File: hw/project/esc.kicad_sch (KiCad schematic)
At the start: 0 parts

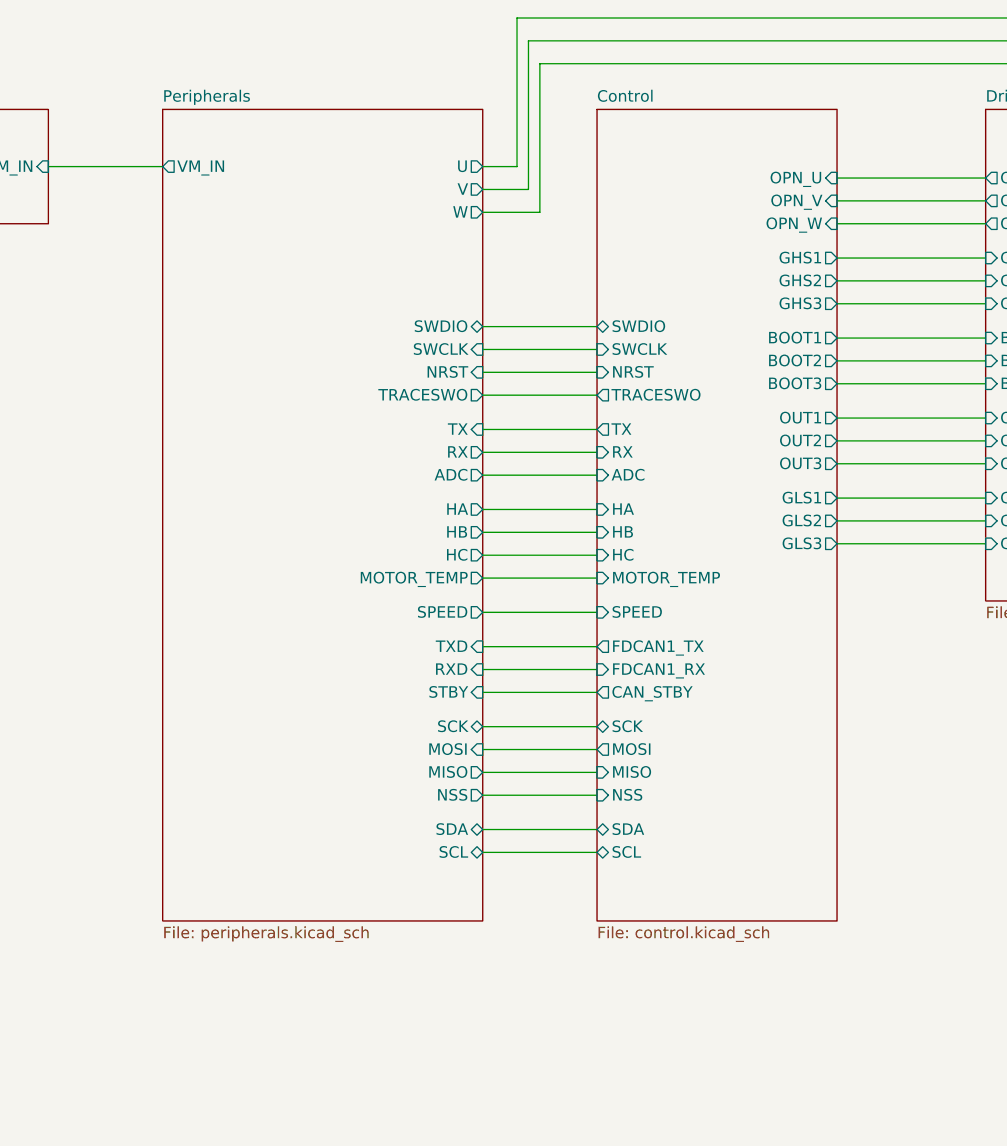
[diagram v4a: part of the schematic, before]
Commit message: Wire up status leds
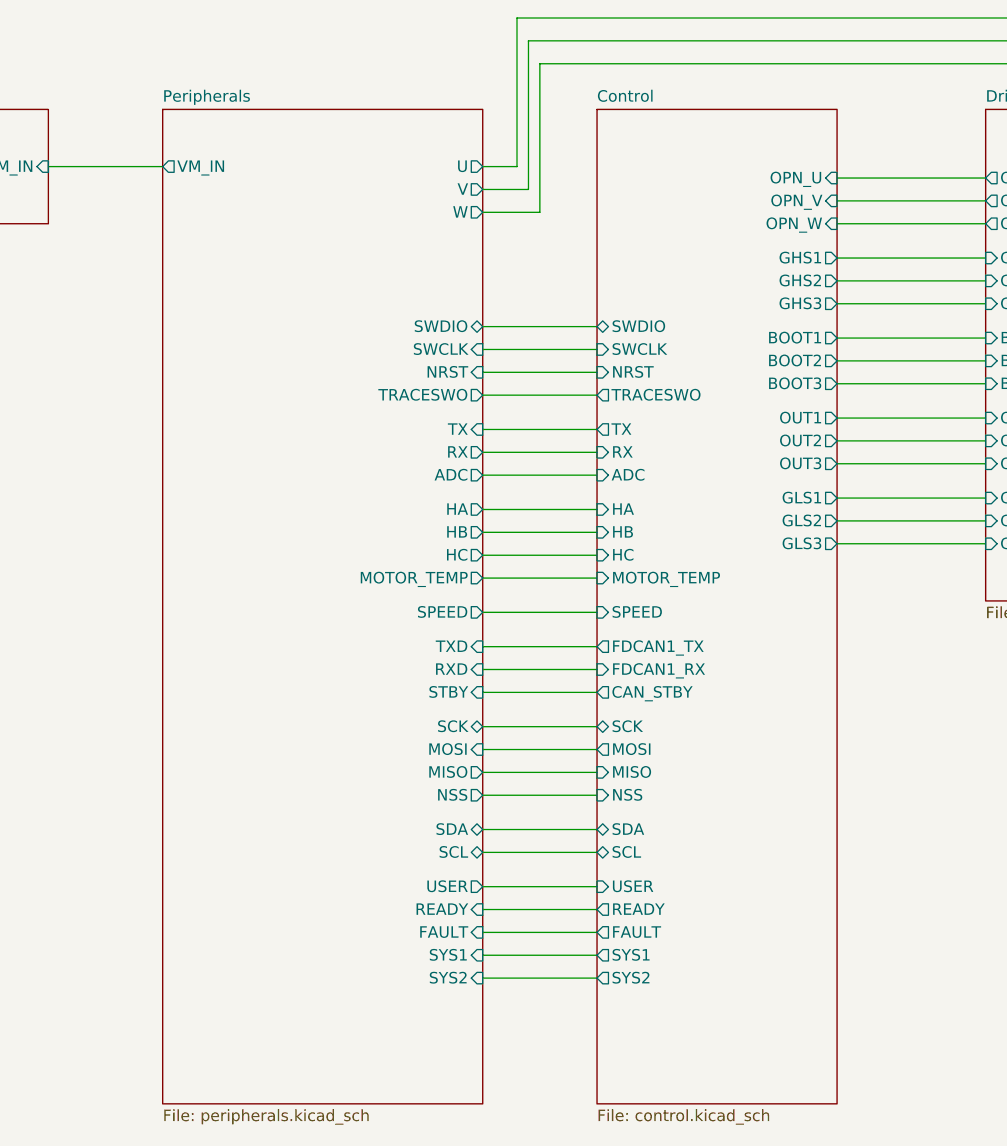
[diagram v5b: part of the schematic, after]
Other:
- sheet Control ports: added FAULT, READY, SYS1, SYS2, USER; removed none
- sheet Peripherals ports: added FAULT, READY, SYS1, SYS2, USER; removed none
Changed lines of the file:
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@@
+	(wire
+		(pts
+			(xy 152.4 156.21) (xy 165.1 156.21)
+		)
+		(stroke
+			(width 0)
+			(type default)
+		)
+	)
 	(wire
 		(pts
@@
 	(wire
 		(pts
+			(xy 152.4 158.75) (xy 165.1 158.75)
+		)
+		(stroke
+			(width 0)
+			(type default)
+		)
+	)
+	(wire
+		(pts
 			(xy 208.28 97.79) (xy 191.77 97.79)
 		)
@@
 	(wire
 		(pts
+			(xy 152.4 161.29) (xy 165.1 161.29)
+		)
+		(stroke
+			(width 0)
+			(type default)
+		)
+	)
+	(wire
+		(pts
 			(xy 157.48 76.2) (xy 152.4 76.2)
 		)
@@
 	(wire
 		(pts
+			(xy 152.4 153.67) (xy 165.1 153.67)
+		)
+		(stroke
+			(width 0)
+			(type default)
+		)
+	)
+	(wire
+		(pts
 			(xy 165.1 93.98) (xy 152.4 93.98)
+		)
+		(stroke
+			(width 0)
+			(type default)
+		)
+	)
+	(wire
+		(pts
+			(xy 152.4 163.83) (xy 165.1 163.83)
 		)
 		(stroke
@@
 	(sheet
 		(at 165.1 67.31)
-		(size 26.67 90.17)
+		(size 26.67 110.49)
 		(exclude_from_sim no)
 		(in_bom yes)
@@
 		)
 		(property "Sheetfile" "control.kicad_sch"
-			(at 165.1 158.0646 0)
+			(at 165.1 178.3846 0)
 			(show_name no)
 			(do_not_autoplace no)
@@
 		(pin "SDA" bidirectional
 			(at 165.1 147.32 180)
+			(effects
+				(font
+					(size 1.27 1.27)
+				)
+				(justify left)
+			)
+		)
+		(pin "SYS2" output
+			(at 165.1 163.83 180)
+			(effects
+				(font
+					(size 1.27 1.27)
+				)
+				(justify left)
+			)
+		)
+		(pin "SYS1" output
+			(at 165.1 161.29 180)
+			(effects
+				(font
+					(size 1.27 1.27)
+				)
+				(justify left)
+			)
+		)
+		(pin "FAULT" output
+			(at 165.1 158.75 180)
+			(effects
+				(font
+					(size 1.27 1.27)
+				)
+				(justify left)
+			)
+		)
+		(pin "USER" input
+			(at 165.1 153.67 180)
+			(effects
+				(font
+					(size 1.27 1.27)
+				)
+				(justify left)
+			)
+		)
+		(pin "READY" output
+			(at 165.1 156.21 180)
 			(effects
 				(font
@@
 	(sheet
 		(at 116.84 67.31)
-		(size 35.56 90.17)
+		(size 35.56 110.49)
 		(exclude_from_sim no)
 		(in_bom yes)
@@
 		)
 		(property "Sheetfile" "peripherals.kicad_sch"
-			(at 116.84 158.0646 0)
+			(at 116.84 178.3846 0)
 			(show_name no)
 			(do_not_autoplace no)
@@
 			(effects
 				(font
+					(size 1.27 1.27)
+				)
+				(justify right)
+			)
+		)
+		(pin "USER" output
+			(at 152.4 153.67 0)
+			(effects
+				(font
+					(size 1.27 1.27)
+				)
+				(justify right)
+			)
+		)
+		(pin "SYS1" input
+			(at 152.4 161.29 0)
+			(effects
+				(font
+					(size 1.27 1.27)
+				)
+				(justify right)
+			)
+		)
+		(pin "SYS2" input
+			(at 152.4 163.83 0)
+			(effects
+				(font
+					(size 1.27 1.27)
+				)
+				(justify right)
+			)
+		)
+		(pin "READY" input
+			(at 152.4 156.21 0)
+			(effects
+				(font
+					(size 1.27 1.27)
+				)
+				(justify right)
+			)
+		)
+		(pin "FAULT" input
+			(at 152.4 158.75 0)
+			(effects
+				(font

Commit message: stm header and minor changes
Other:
- sheet Control ports: added PA1, PA2, PA8, PB1, PB6, PB7, PC2; removed none

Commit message: minor changes
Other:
- sheet Control ports: added PWR_BTN; removed PB1, PB6
- sheet Peripherals ports: added PA1, PA2, PA8, PB7, PC2, PWR_BTN; removed none
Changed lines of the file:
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@@
+	(wire
+		(pts
+			(xy 118.11 154.94) (xy 130.81 154.94)
+		)
+		(stroke
+			(width 0)
+			(type default)
+		)
+	)
 	(wire
 		(pts
@@
 	(wire
 		(pts
+			(xy 118.11 158.75) (xy 130.81 158.75)
+		)
+		(stroke
+			(width 0)
+			(type default)
+		)
+	)
+	(wire
+		(pts
 			(xy 173.99 54.61) (xy 157.48 54.61)
 		)
@@
 	(wire
 		(pts
+			(xy 118.11 139.7) (xy 130.81 139.7)
+		)
+		(stroke
+			(width 0)
+			(type default)
+		)
+	)
+	(wire
+		(pts
 			(xy 189.23 27.94) (xy 121.92 27.94)
 		)
@@
 	(wire
 		(pts
+			(xy 118.11 147.32) (xy 130.81 147.32)
+		)
+		(stroke
+			(width 0)
+			(type default)
+		)
+	)
+	(wire
+		(pts
 			(xy 123.19 46.99) (xy 118.11 46.99)
 		)
@@
 	(wire
 		(pts
+			(xy 118.11 144.78) (xy 130.81 144.78)
+		)
+		(stroke
+			(width 0)
+			(type default)
+		)
+	)
+	(wire
+		(pts
 			(xy 130.81 64.77) (xy 118.11 64.77)
 		)
@@
 		(pts
 			(xy 118.11 134.62) (xy 130.81 134.62)
+		)
+		(stroke
+			(width 0)
+			(type default)
+		)
+	)
+	(wire
+		(pts
+			(xy 118.11 152.4) (xy 130.81 152.4)
 		)
 		(stroke
@@
 			)
 		)
-		(pin "PB1" input
-			(at 130.81 142.24 180)
-			(effects
-				(font
-					(size 1.27 1.27)
-				)
-				(justify left)
-			)
-		)
 		(pin "PA1" input
 			(at 130.81 144.78 180)
@@
 			)
 		)
-		(pin "PB6" input
-			(at 130.81 149.86 180)
-			(effects
-				(font
-					(size 1.27 1.27)
-				)
-				(justify left)
-			)
-		)
 		(pin "PA8" input
 			(at 130.81 152.4 180)
@@
 		(pin "PC2" input
 			(at 130.81 154.94 180)
+			(effects
+				(font
+					(size 1.27 1.27)
+				)
+				(justify left)
+			)
+		)
+		(pin "PWR_BTN" input
+			(at 130.81 158.75 180)
 			(effects
 				(font
@@
 			(effects
 				(font
+					(size 1.27 1.27)
+				)
+				(justify right)
+			)
+		)
+		(pin "PA1" input
+			(at 118.11 144.78 0)
+			(effects
+				(font
+					(size 1.27 1.27)
+				)
+				(justify right)
+			)
+		)
+		(pin "PC2" input
+			(at 118.11 154.94 0)
+			(effects
+				(font
+					(size 1.27 1.27)
+				)
+				(justify right)
+			)
+		)
+		(pin "PA2" input
+			(at 118.11 139.7 0)
+			(effects
+				(font
+					(size 1.27 1.27)
+				)
+				(justify right)
+			)
+		)
+		(pin "PA8" input
+			(at 118.11 152.4 0)
+			(effects
+				(font
+					(size 1.27 1.27)
+				)
+				(justify right)
+			)
+		)
+		(pin "PB7" input
+			(at 118.11 147.32 0)
+			(effects
+				(font
+					(size 1.27 1.27)
+				)
+				(justify right)
+			)
+		)
+		(pin "PWR_BTN" output
+			(at 118.11 158.75 0)
+			(effects
+				(font

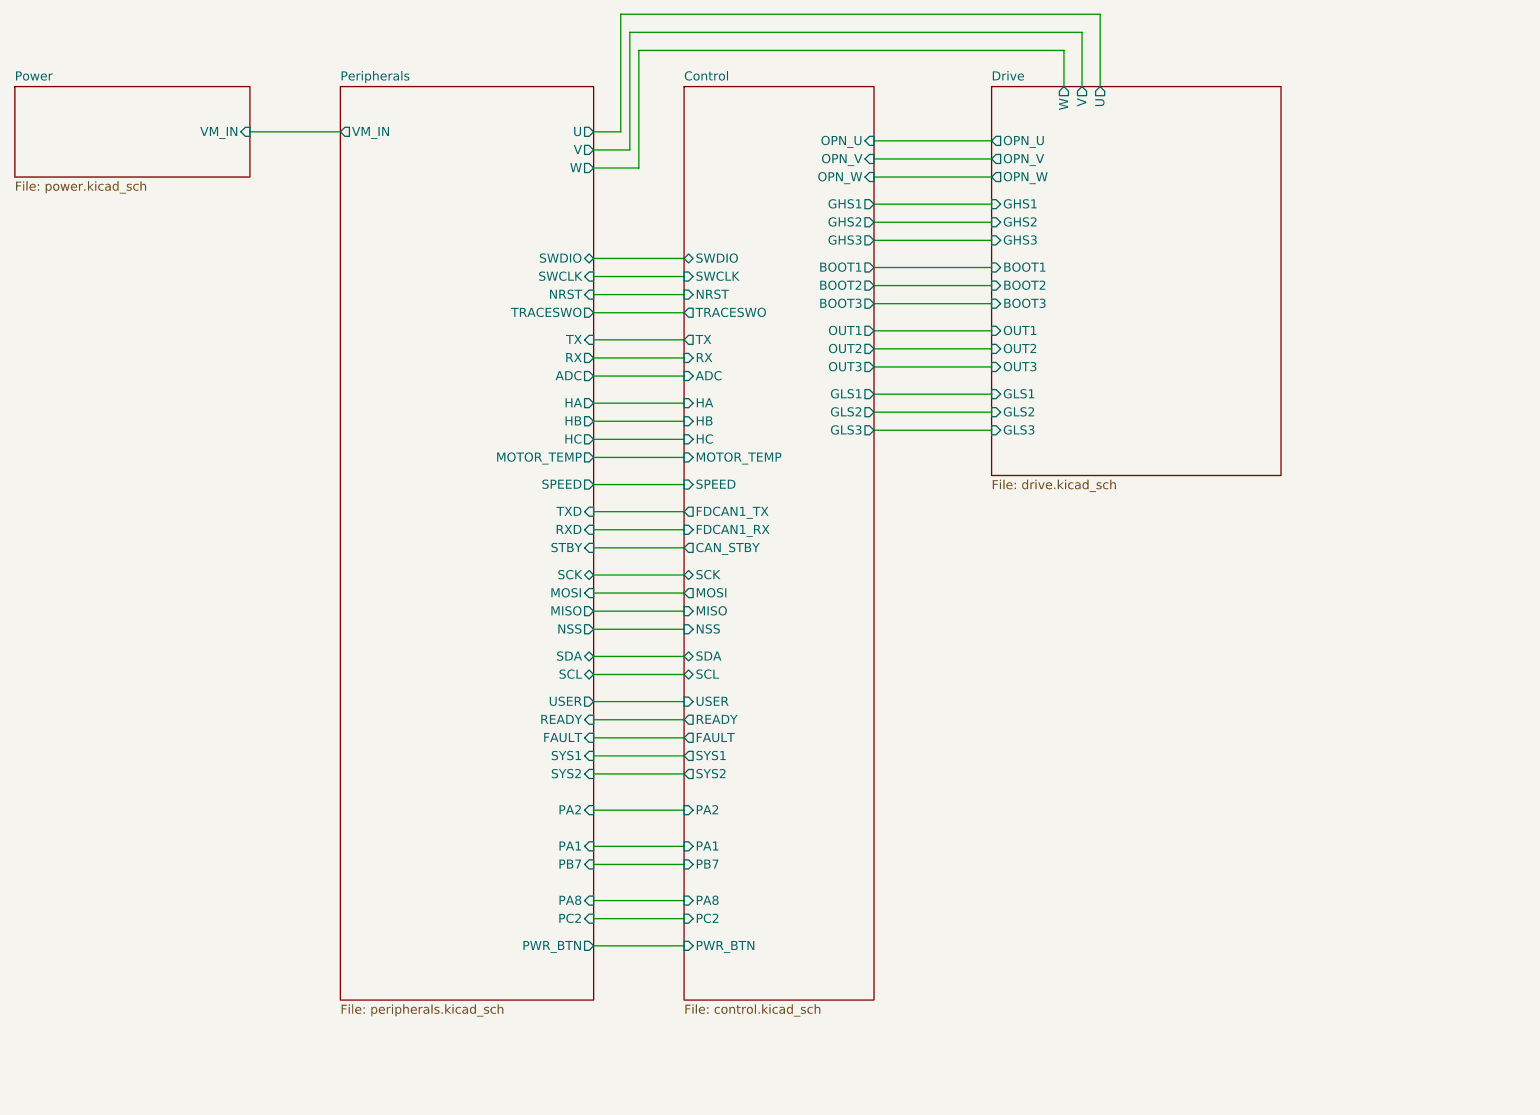
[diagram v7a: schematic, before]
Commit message: Wire PWR BTN
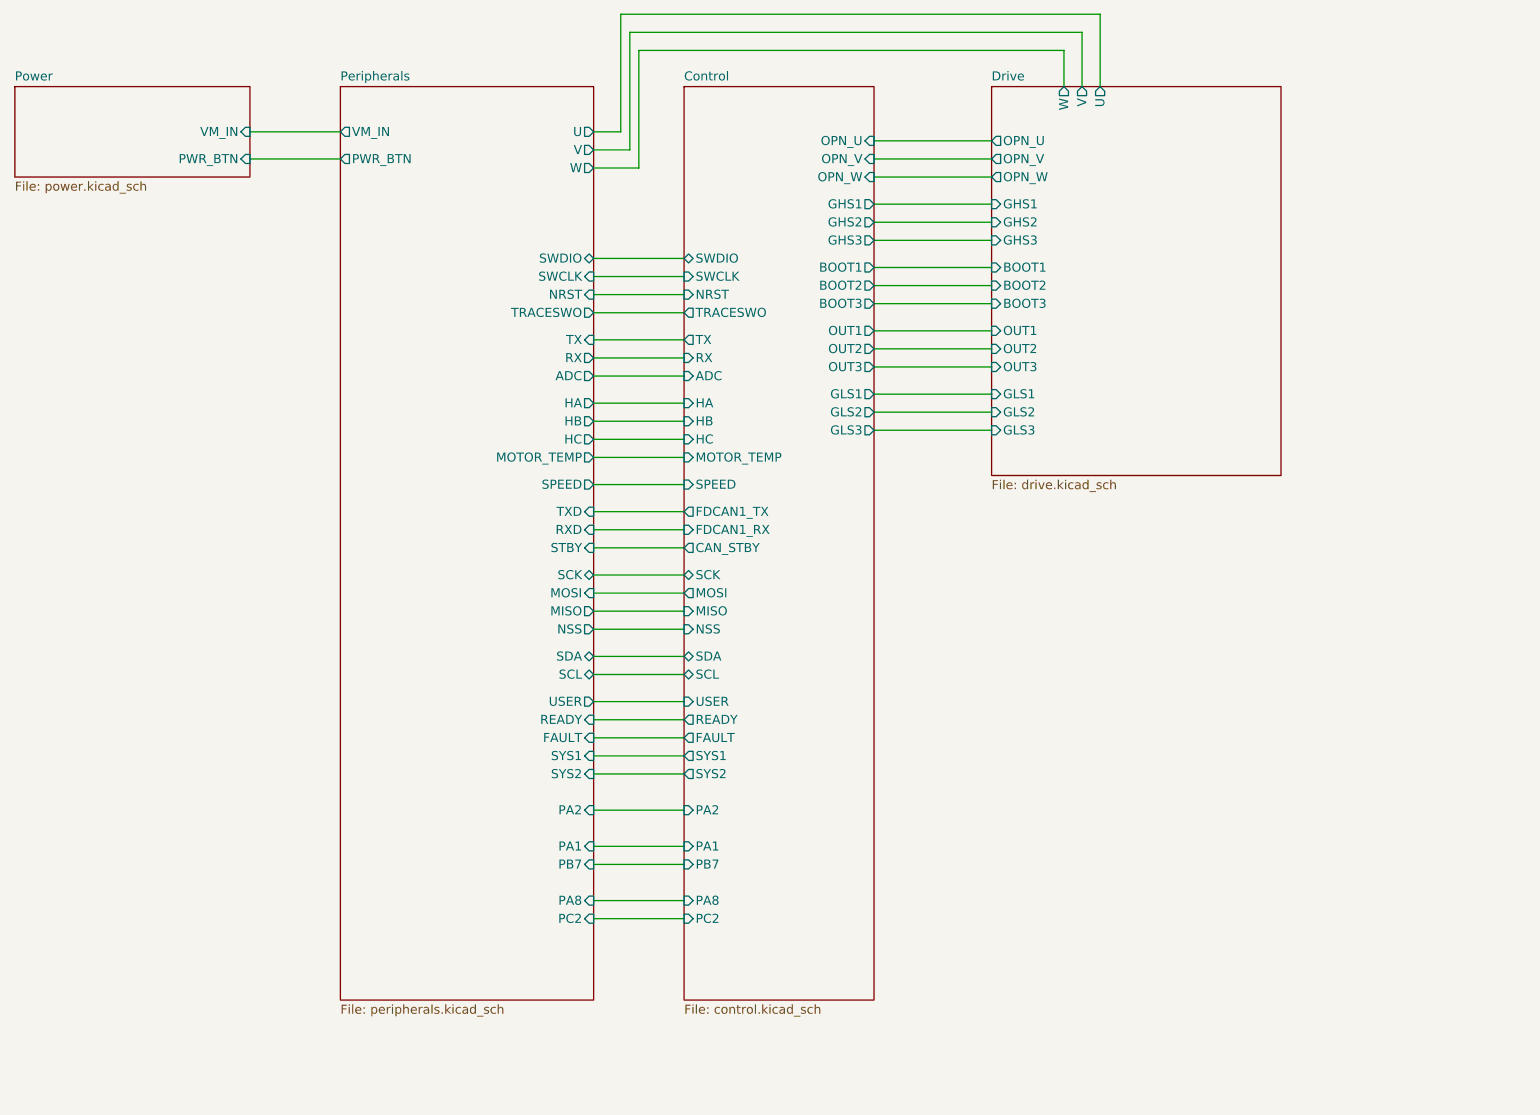
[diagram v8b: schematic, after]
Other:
- sheet Control ports: added none; removed PWR_BTN
- sheet Power ports: added PWR_BTN; removed none
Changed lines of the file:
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@@
-	(wire
-		(pts
-			(xy 118.11 158.75) (xy 130.81 158.75)
-		)
-		(stroke
-			(width 0)
-			(type default)
-		)
-	)
 	(wire
 		(pts
@@
 		(pts
 			(xy 118.11 152.4) (xy 130.81 152.4)
+		)
+		(stroke
+			(width 0)
+			(type default)
+		)
+	)
+	(wire
+		(pts
+			(xy 69.85 48.26) (xy 82.55 48.26)
 		)
 		(stroke
@@
 			)
 		)
-		(pin "PWR_BTN" input
-			(at 130.81 158.75 180)
-			(effects
-				(font
-					(size 1.27 1.27)
-				)
-				(justify left)
-			)
-		)
 		(instances
 			(project "esc"
@@
 			)
 		)
+		(pin "PWR_BTN" input
+			(at 69.85 48.26 0)
+			(effects
+				(font
+					(size 1.27 1.27)
+				)
+				(justify right)
+			)
+		)
 		(instances
 			(project "esc"
@@
 		)
 		(pin "PWR_BTN" output
-			(at 118.11 158.75 0)
-			(effects
-				(font
-					(size 1.27 1.27)
-				)
-				(justify right)
-			)
-		)
+			(at 82.55 48.26 180)
+			(effects
+				(font
+					(size 1.27 1.27)
+				)
+				(justify left)
+			)
+		)
